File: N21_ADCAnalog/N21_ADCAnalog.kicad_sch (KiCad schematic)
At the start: 9 parts

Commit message: WIP
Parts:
- removed TP2012: TestPoint, Connector_PinHeader_1.00mm:PinHeader_1x01_P1.00mm_Vertical, symbol Connector:TestPoint
- added A2101: LF356N, symbol Amplifier_Operational:LF356
- added A2102: LM201AN, Package_SO:MSOP-8_3x3mm_P0.65mm, symbol Amplifier_Operational:AD8021ARM
- added C2101: 10n, symbol Device:C
- added C2102: xn, symbol Device:C
- added C2103: 162n, symbol Device:C
- added C2104: 3u1, symbol Device:C
- added C2105: 33p, symbol Device:C
- added C2110, C2111: 4n7, symbol Device:C
- added D2101: HEF4066, symbol 4xxx:4066
- added D2104: HEF4104, symbol 4xxx_IEEE:4104
- added R2101: 8K66, symbol Device:R
- added R2102: 140k, symbol Device:R
- added R2103: 64k9, symbol Device:R
- added R2103: 24k9, symbol Device:R
- added R2104: 680k, symbol Device:R_Potentiometer
- added R2105, R2106: 82k5, symbol Device:R
- added R2108: 40k2, symbol Device:R
- added R21xx: 5k90, symbol Device:R
- added TP2104, TP2105, TP2106, TP2109: TestPoint, symbol Connector:TestPoint
- added V2101A, V2101B: BF244A, Package_TO_SOT_THT:TO-92_Inline, symbol Transistor_FET:BF244A
- added V2102: BSV80, Package_TO_SOT_THT:TO-92_Inline, symbol Transistor_FET:BF244A
- added V2103, V2104, V2105: BAW62, symbol Device:D
- renumbered TP2013 to TP2103
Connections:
- net +15V: now also A2101.7 (V+), A2102.7 (V+), C2101.1, R2103.1
- net +2VRef: now also C2110.1, D2101.11
- net +5V: now also D2104.1 (Vddo)
- net -15V: now also A2101.4 (V-), A2102.4 (V-), C2102.1, R2105.2, R2106.2
- net -5V: now also D2101.7 (VSS), D2104.8 (Vss)
- net AZ: now also D2104.5
- net DN+: now also D2104.12
- net DN-: now also D2104.4
- net GND3: now also C2104.2, C2110.2, C2111.1, D2101.4, D2104.15 (EN), D2104.16 (Vddi)
- net GND4: now also C2101.2, C2102.2, D2101.14 (VDD), R2108.2, V2104.1 (K), V2105.2 (A)
- net INPUT: now also R2101.1, TP2109.1
- net UP: now also D2104.11
- new net: D2101.1, R2101.2
- new net: A2101.3 (+), D2101.10, D2101.2, D2101.3, D2101.9, TP2104.1
- new net: R2103.2, V2101A.1 (D), V2101B.1 (D)
- new net: C2103.2, R2102.1, V2101A.2 (G)
- new net: A2102.2 (-), R2105.1, V2101A.3 (S)
- new net: C2111.2, D2101.8
- new net: A2102.3 (+), R2106.1, V2101B.3 (S)
- new net: R21xx.1, V2102.1 (D), V2104.2 (A), V2105.1 (K)
- new net: A2102.6, C2103.1, TP2106.1
- new net: R2108.1, V2102.2 (G), V2103.2 (A)
- new net: C2104.1, V2101B.2 (G), V2102.3 (S)
- new net: A2101.2 (-), A2101.6, R2102.2, R2103.1, TP2105.1
- new net: A2102.1 (LOGIC_REFERENCE), C2105.1
- new net: A2102.8 (~{DISABLE}), C2105.2
- new net: R2103.2, R2104.1
- new net: R2104.2, R2104.3
- new net SAZ: D2101.5, D2104.6
- new net SDN+: D2101.12, D2104.13
- new net SDN-: D2101.6, D2104.3
- new net SUP: D2101.13, D2104.10
- no-connect marks 3 -> 10
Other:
- note added: "Buffer"
- note added: "Integrator"
- note added: "Level shift"

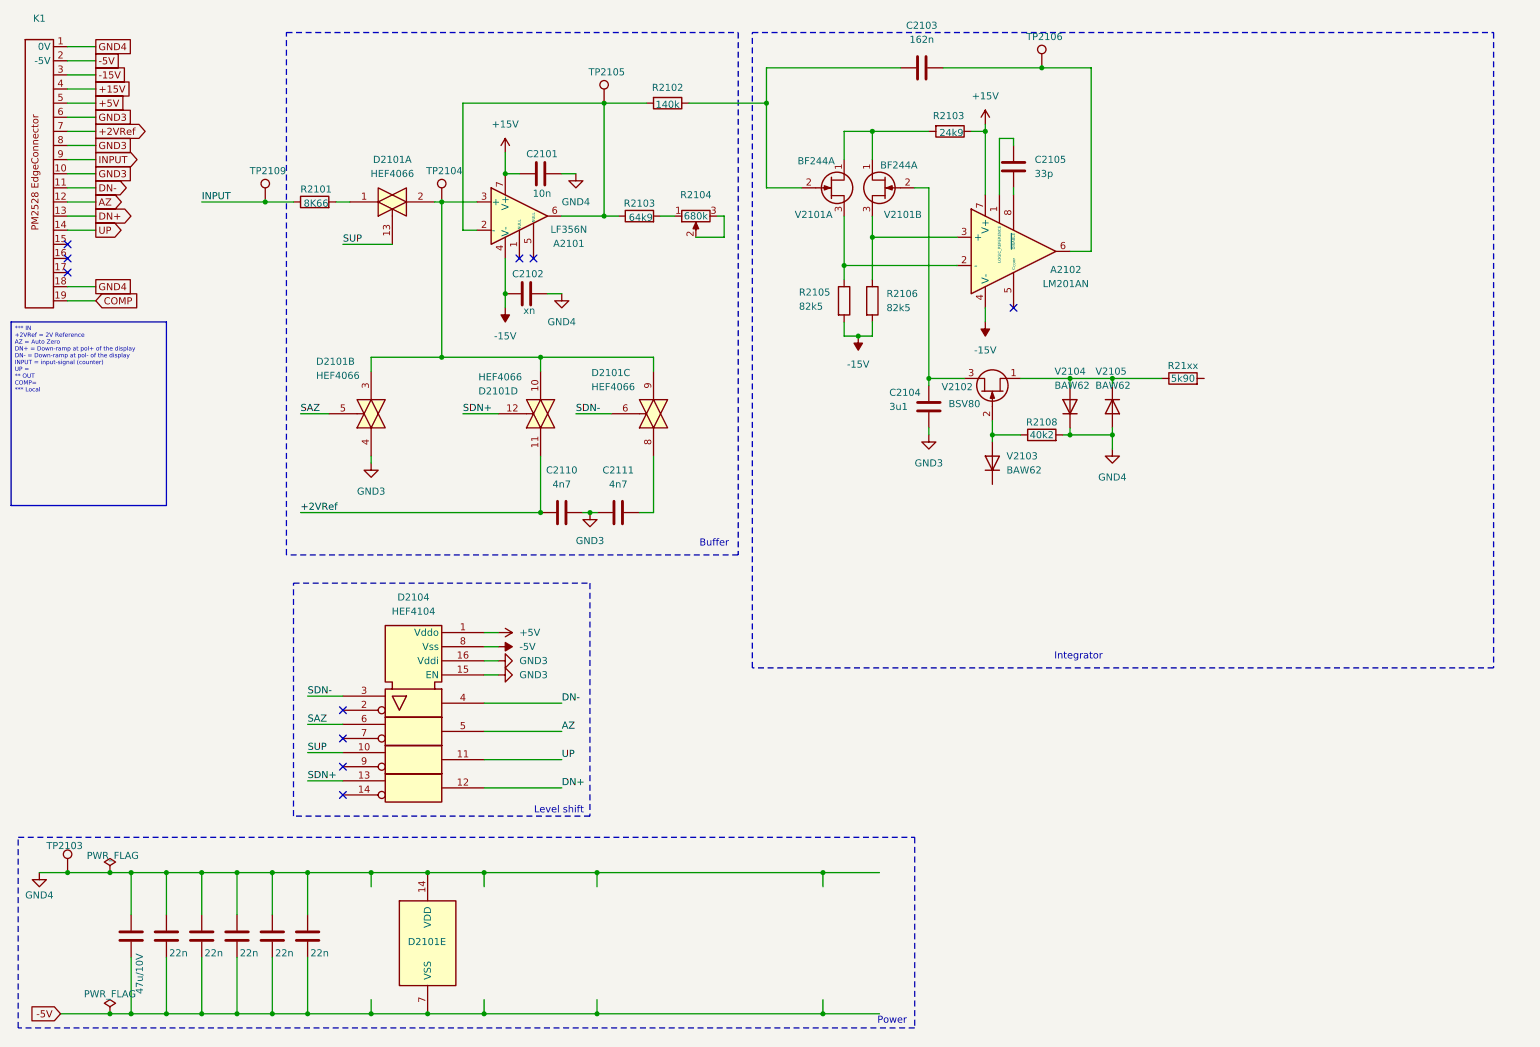
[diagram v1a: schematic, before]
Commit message: Replaced testpins with testloops/beads
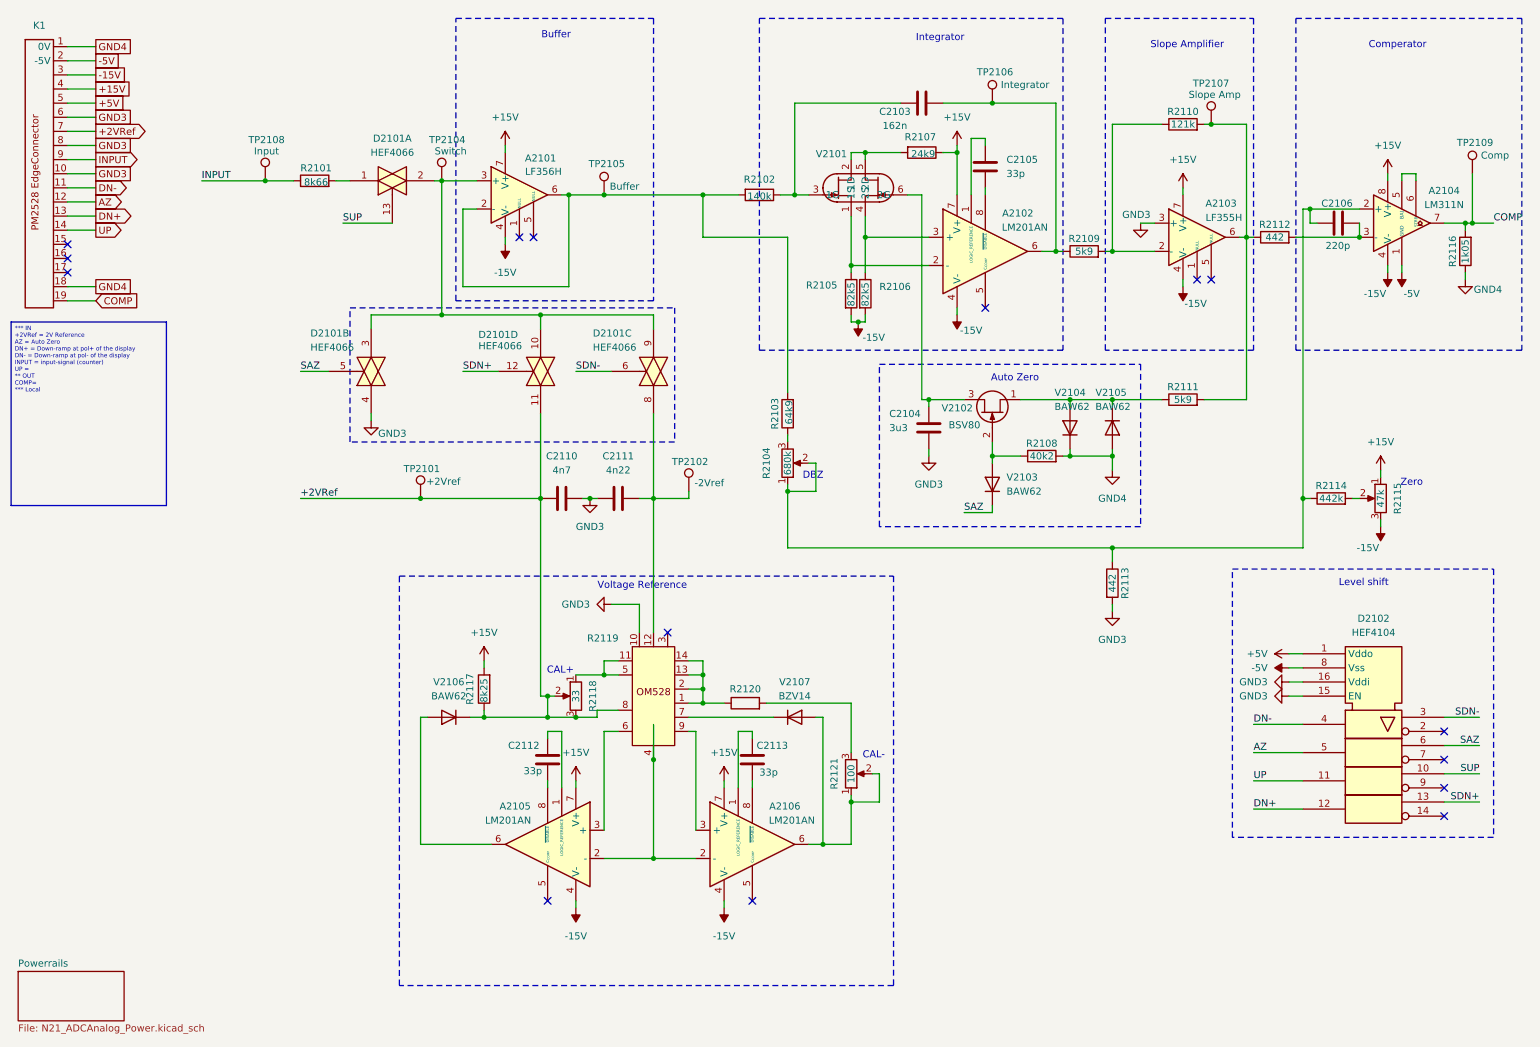
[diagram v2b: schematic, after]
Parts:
- removed C2001, C2002, C2003, C2004, C2005: 22n, Capacitor_THT:C_Rect_L7.0mm_W2.0mm_P5.00mm, symbol Device:C
- removed C2007: 47u/10V, Capacitor_THT:CP_Axial_L10.0mm_D6.0mm_P15.00mm_Horizontal, symbol Device:C
- removed C2101: 10n, symbol Device:C
- removed C2102: xn, symbol Device:C
- removed unit 5 of D2101
- removed TP2103: TestPoint, Connector_PinHeader_1.00mm:PinHeader_1x01_P1.00mm_Vertical, symbol Connector:TestPoint
- removed V2101A, V2101B: BF244A, Package_TO_SOT_THT:TO-92_Inline, symbol Transistor_FET:BF244A
- added A2103: LF355H, Package_DIP:DIP-8_W7.62mm, symbol Amplifier_Operational:LF355
- added A2104: LM311N, symbol Comparator:LM311
- added A2105, A2106: LM201AN, Package_DIP:DIP-8_W7.62mm, symbol Amplifier_Operational:AD8021ARM
- added C2106: 220p, Capacitor_THT:C_Disc_D4.3mm_W1.9mm_P5.00mm, symbol Device:C
- added C2112, C2113: 33p, Capacitor_THT:C_Disc_D4.3mm_W1.9mm_P5.00mm, symbol Device:C
- added R2109: 5k9, Resistor_THT:R_Axial_DIN0207_L6.3mm_D2.5mm_P10.16mm_Horizontal, symbol Device:R
- added R2110: 121k, Resistor_THT:R_Axial_DIN0207_L6.3mm_D2.5mm_P10.16mm_Horizontal, symbol Device:R
- added R2112, R2113: 442, Resistor_THT:R_Axial_DIN0207_L6.3mm_D2.5mm_P10.16mm_Horizontal, symbol Device:R
- added R2114: 442k, Resistor_THT:R_Axial_DIN0207_L6.3mm_D2.5mm_P10.16mm_Horizontal, symbol Device:R
- added R2115: 47k, Potentiometer_THT:Potentiometer_Bourns_3296Y_Vertical, symbol Device:R_Potentiometer
- added R2116: 1k05, Resistor_THT:R_Axial_DIN0207_L6.3mm_D2.5mm_P10.16mm_Horizontal, symbol Device:R
- added R2117: 8k25, Resistor_THT:R_Axial_DIN0207_L6.3mm_D2.5mm_P10.16mm_Horizontal, symbol Device:R
- added R2118: 33, Potentiometer_THT:Potentiometer_Bourns_3296Y_Vertical, symbol Device:R_Potentiometer
- added R2119: ~, Package_DIP:DIP-16_W7.62mm, symbol PM2528:OM528
- added R2120: ~, symbol Device:R
- added R2121: 100, Potentiometer_THT:Potentiometer_Bourns_3296Y_Vertical, symbol Device:R_Potentiometer
- added TP2101: +2Vref, Connector_Pin:Pin_D1.0mm_L10.0mm, symbol Connector:TestPoint
- added TP2102: -2Vref, Connector_Pin:Pin_D1.0mm_L10.0mm, symbol Connector:TestPoint
- added TP2107: Slope Amp, Connector_Pin:Pin_D1.0mm_L10.0mm, symbol Connector:TestPoint
- added TP2109: Comp, Connector_Pin:Pin_D1.0mm_L10.0mm, symbol Connector:TestPoint
- added V2101: ~, symbol PM2528:ON528
- added V2106: BAW62, Diode_THT:D_DO-34_SOD68_P10.16mm_Horizontal, symbol Device:D
- added V2107: BZV14, Diode_THT:D_DO-34_SOD68_P10.16mm_Horizontal, symbol Device:D
- A2101: value LF356N -> LF356H; footprint (none) -> Package_DIP:DIP-8_W7.62mm
- A2102: footprint Package_SO:MSOP-8_3x3mm_P0.65mm -> Package_DIP:DIP-8_W7.62mm
- C2103: footprint (none) -> Capacitor_THT:CP_Axial_L25.0mm_D10.0mm_P30.00mm_Horizontal
- C2104: value 3u1 -> 3u3; footprint (none) -> Capacitor_THT:C_Rect_L26.5mm_W8.5mm_P22.50mm_MKS4
- C2105, C2110: footprint (none) -> Capacitor_THT:C_Disc_D4.3mm_W1.9mm_P5.00mm
- C2111: value 4n7 -> 4n22
- D2101: footprint (none) -> Package_DIP:DIP-14_W7.62mm
- D2102: renamed from D2104; footprint (none) -> Package_DIP:DIP-16_W7.62mm
- K1: symbol _PhilipsPM2528DMM:PCBEdge_Plugincard -> PM2528:PCBEdge_Plugincard
- R2101: value 8K66 -> 8k66; footprint (none) -> Resistor_THT:R_Axial_DIN0207_L6.3mm_D2.5mm_P10.16mm_Horizontal
- R2102, R2103, R2105, R2106, R2108: footprint (none) -> Resistor_THT:R_Axial_DIN0207_L6.3mm_D2.5mm_P10.16mm_Horizontal
- R2104: footprint (none) -> Potentiometer_THT:Potentiometer_Bourns_3296Y_Vertical
- R2107: renamed from R2103; footprint (none) -> Resistor_THT:R_Axial_DIN0207_L6.3mm_D2.5mm_P10.16mm_Horizontal
- R2111: renamed from R21xx; value 5k90 -> 5k9; footprint (none) -> Resistor_THT:R_Axial_DIN0207_L6.3mm_D2.5mm_P10.16mm_Horizontal
- TP2104: value TestPoint -> Switch; footprint (none) -> Connector_Pin:Pin_D1.0mm_L10.0mm
- TP2105: value TestPoint -> Buffer; footprint (none) -> Connector_Pin:Pin_D1.0mm_L10.0mm
- TP2106: value TestPoint -> Integrator; footprint (none) -> Connector_Pin:Pin_D1.0mm_L10.0mm
- TP2108: renamed from TP2109; value TestPoint -> Input; footprint (none) -> Connector_Pin:Pin_D1.0mm_L10.0mm
- V2103, V2104, V2105: footprint (none) -> Diode_THT:D_DO-34_SOD68_P10.16mm_Horizontal
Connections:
- net +15V: now also A2103.7 (V+), A2104.8 (V+), A2105.7 (V+), A2106.7 (V+), R2115.1, R2117.2
- net +2VRef: now also R2117.1, R2118.2, R2118.3, R2119.8, TP2101.1, V2106.1 (K)
- net -15V: now also A2103.4 (V-), A2104.4 (V-), A2105.4 (V-), A2106.4 (V-), R2115.3
- net -5V: now also A2104.1 (GND)
- net COMP: now also A2104.7, R2116.2, TP2109.1
- net GND3: now also A2103.3 (+), R2113.2, R2119.10
- net GND4: now also R2116.1
- net SAZ: now also V2103.1 (K)
- net at R2107.2: now also V2101.2 (1D), V2101.5 (2D)
- net at C2103.2, R2102.1: now also V2101.3 (1G)
- net at A2102.2 (-), R2105.1: now also V2101.1 (1S)
- net at C2111.2, D2101.8: now also R2119.12, TP2102.1
- net at A2102.3 (+), R2106.1: now also V2101.4 (2S)
- net at A2102.6, C2103.1, TP2106.1: now also R2109.1
- net at C2104.1, V2102.3 (S): now also V2101.6 (2G)
- net at A2101.2 (-), A2101.6, R2102.2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: now also R2103.2; no longer R2103.1
- net at R2104.1: now also R2104.2, A2104.2 (+), C2106.2, R2113.1, R2114.1; no longer R2103.2
- net at R2104.3: now also R2103.1; no longer R2104.2
- net at R2111.2: now also A2103.6, R2110.2, R2112.1, TP2107.1
- new net: R2114.2, R2115.2
- new net: A2103.2 (-), R2109.2, R2110.1
- new net: A2106.1 (LOGIC_REFERENCE), C2113.2
- new net: A2105.2 (-), A2106.2 (-), R2119.4
- new net: A2106.3 (+), R2119.9
- new net: A2106.6, R2121.1, R2121.2, V2107.2 (A)
- new net: A2106.8 (~{DISABLE}), C2113.1
- new net: R2119.7, V2107.1 (K)
- new net: R2119.1, R2119.13, R2119.14, R2119.2, R2120.1
- new net: R2118.1, R2119.11, R2119.5
- new net: A2105.3 (+), R2119.6
- new net: R2120.2, R2121.3
- new net: A2104.3 (-), C2106.1, R2112.2
- new net: A2105.1 (LOGIC_REFERENCE), C2112.2
- new net: A2105.6, V2106.2 (A)
- new net: A2105.8 (~{DISABLE}), C2112.1
- new net: A2104.5 (BAL), A2104.6 (STRB)
- no-connect marks 10 -> 15
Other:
- added sheet Powerrails (N21_ADCAnalog_Power.kicad_sch)
- note added: "Auto Zero"
- note added: "CAL+"
- note added: "CAL-"
- note added: "Comperator"
- note added: "DBZ"
- note added: "Slope Amplifier"
- note added: "Voltage Reference"
- note added: "Zero"
- note removed: "Power"
- title: PM2528 N21 (ADC Analog) -> PM2528 N21 (ADC Analog) | Power
- moved on the sheet: A2101, A2102, C2103, C2104, C2105, C2110, C2111, D2101A, D2101B, D2101C, D2101D, D2102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

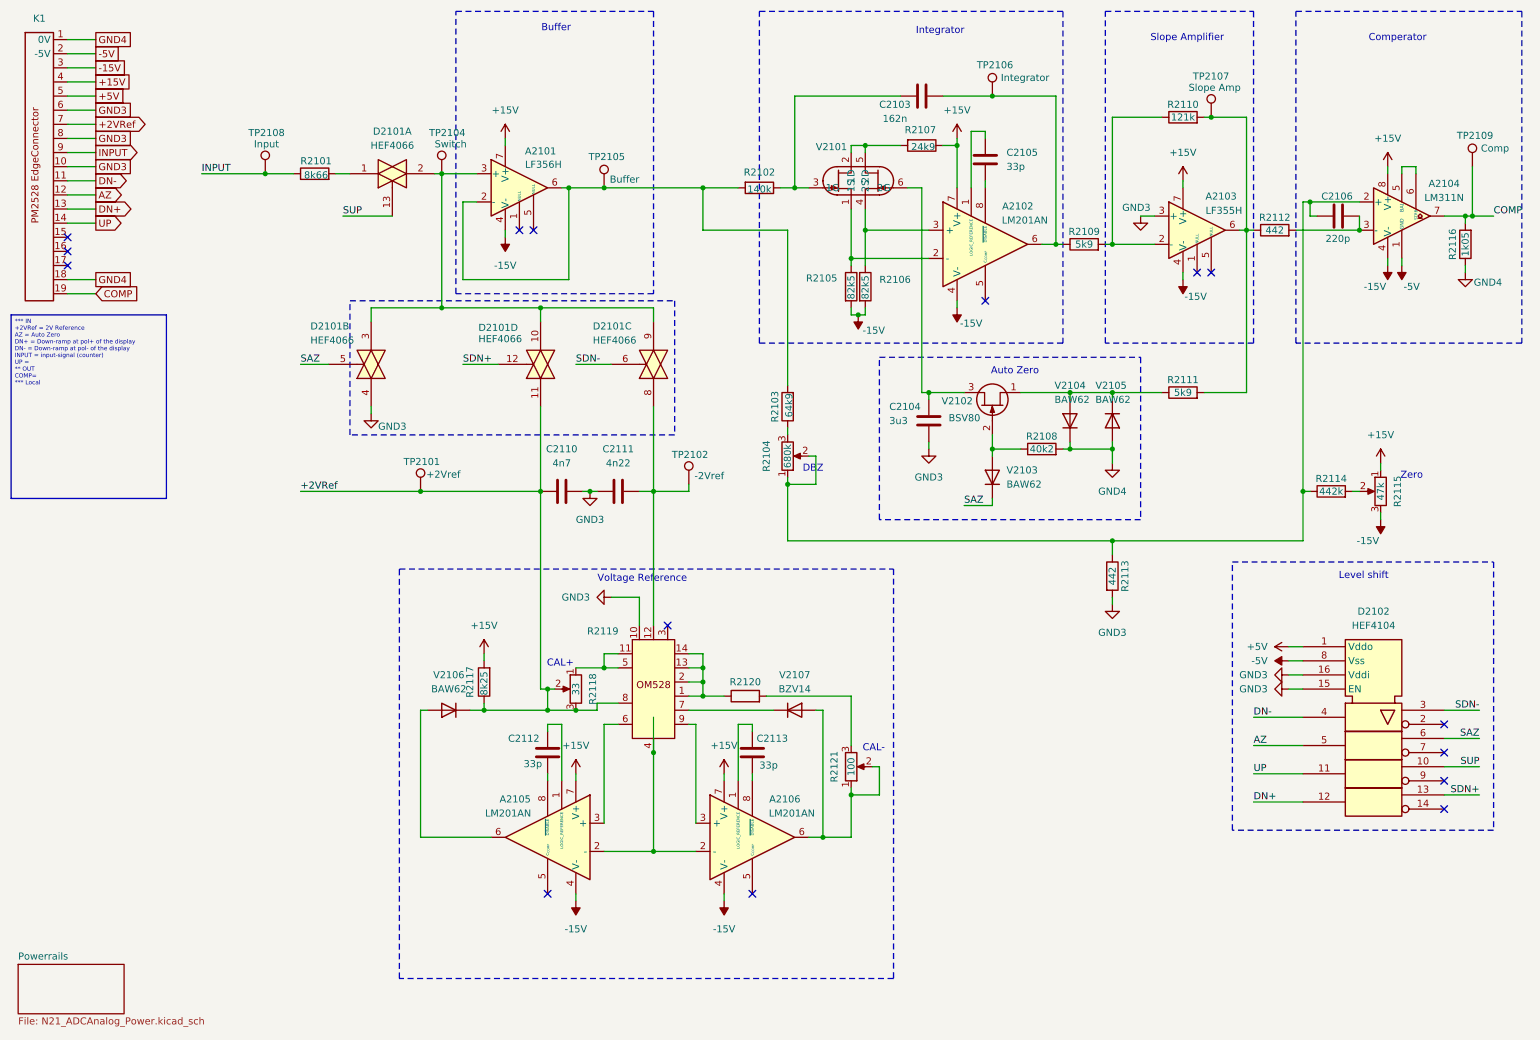
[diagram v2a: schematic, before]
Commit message: Added N22/N23
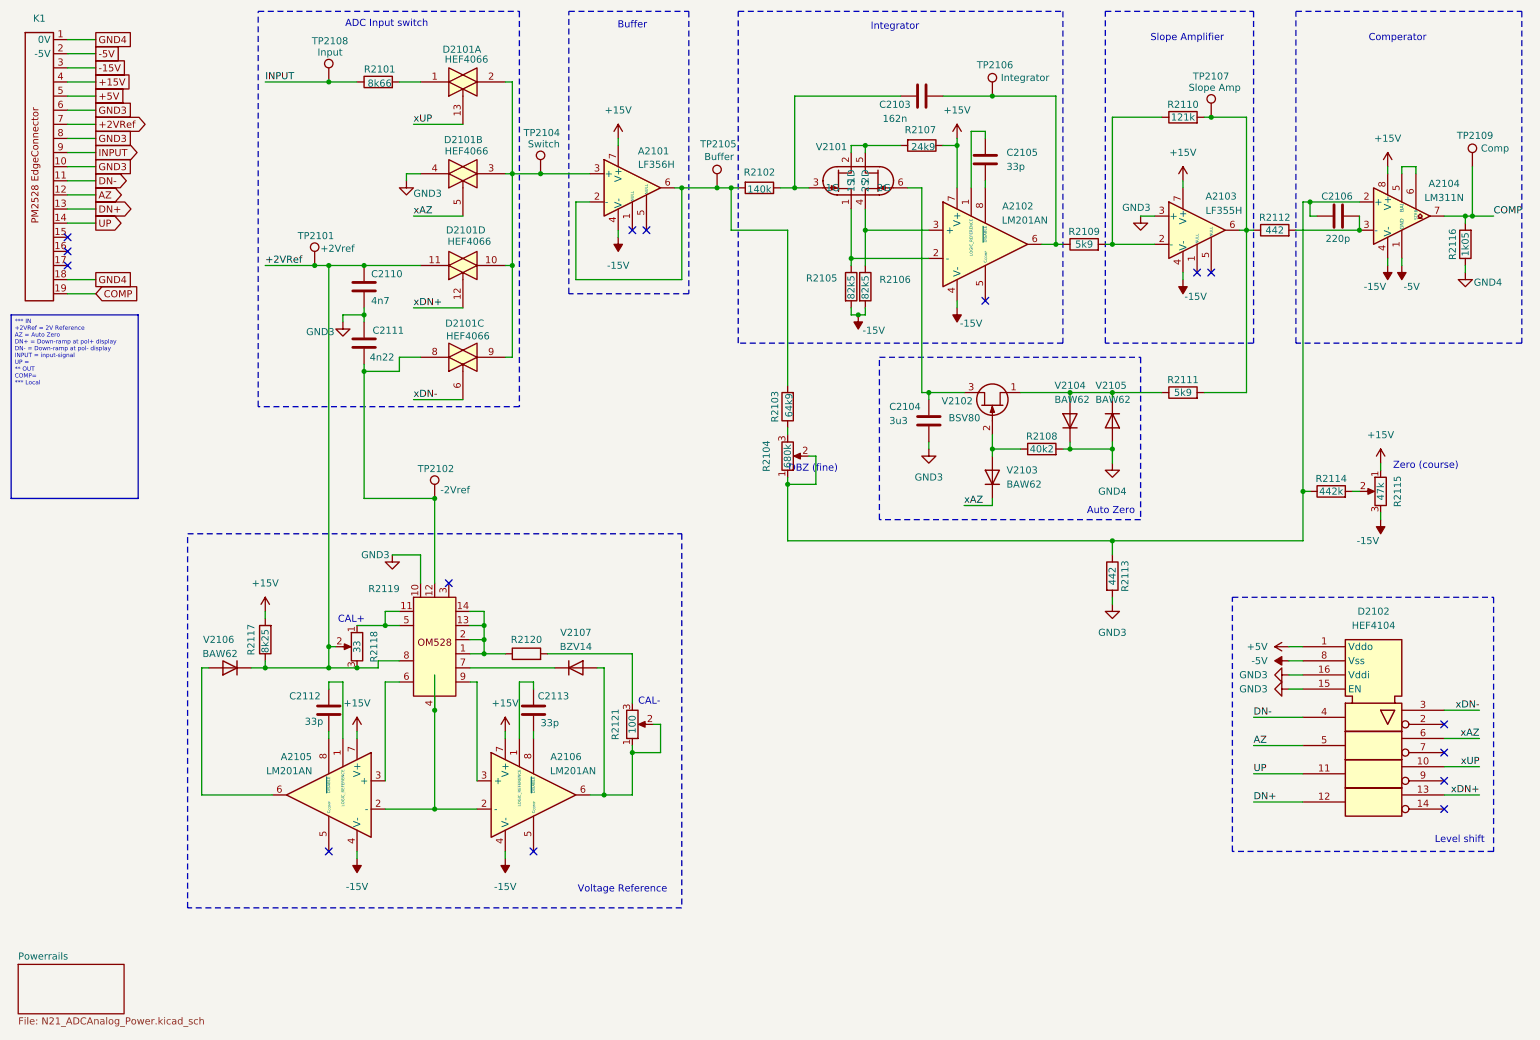
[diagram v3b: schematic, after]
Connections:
- net +2VRef: now also C2110.2; no longer C2110.1
- net GND3: now also C2110.1, C2111.2; no longer C2110.2, C2111.1
- net at D2101.8, R2119.12, TP2102.1: now also C2111.1; no longer C2111.2
- net SAZ renamed xAZ
- net SDN+ renamed xDN+
- net SDN- renamed xDN-
- net SUP renamed xUP
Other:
- note added: "ADC Input switch"
- note added: "DBZ (fine)"
- note added: "Zero (course)"
- note removed: "DBZ"
- note removed: "Zero"
- moved on the sheet: A2101, A2105, A2106, C2110, C2111, C2112, C2113, D2101A, D2101B, D2101C, D2101D, R2101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
